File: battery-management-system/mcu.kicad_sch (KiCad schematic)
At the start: 44 parts, among them J16 I2C, J17 UART_INTERCONNECT, J18 LEDS, J19 CHARGE/DISCHARGE, J20 UART_USB, Q5 DMN3404L, U10 STC3100, U11 STM32L071CZTx, U7 ARM-JTAG-SWD, U8 AT24C512C, U9 NCT75DR2G

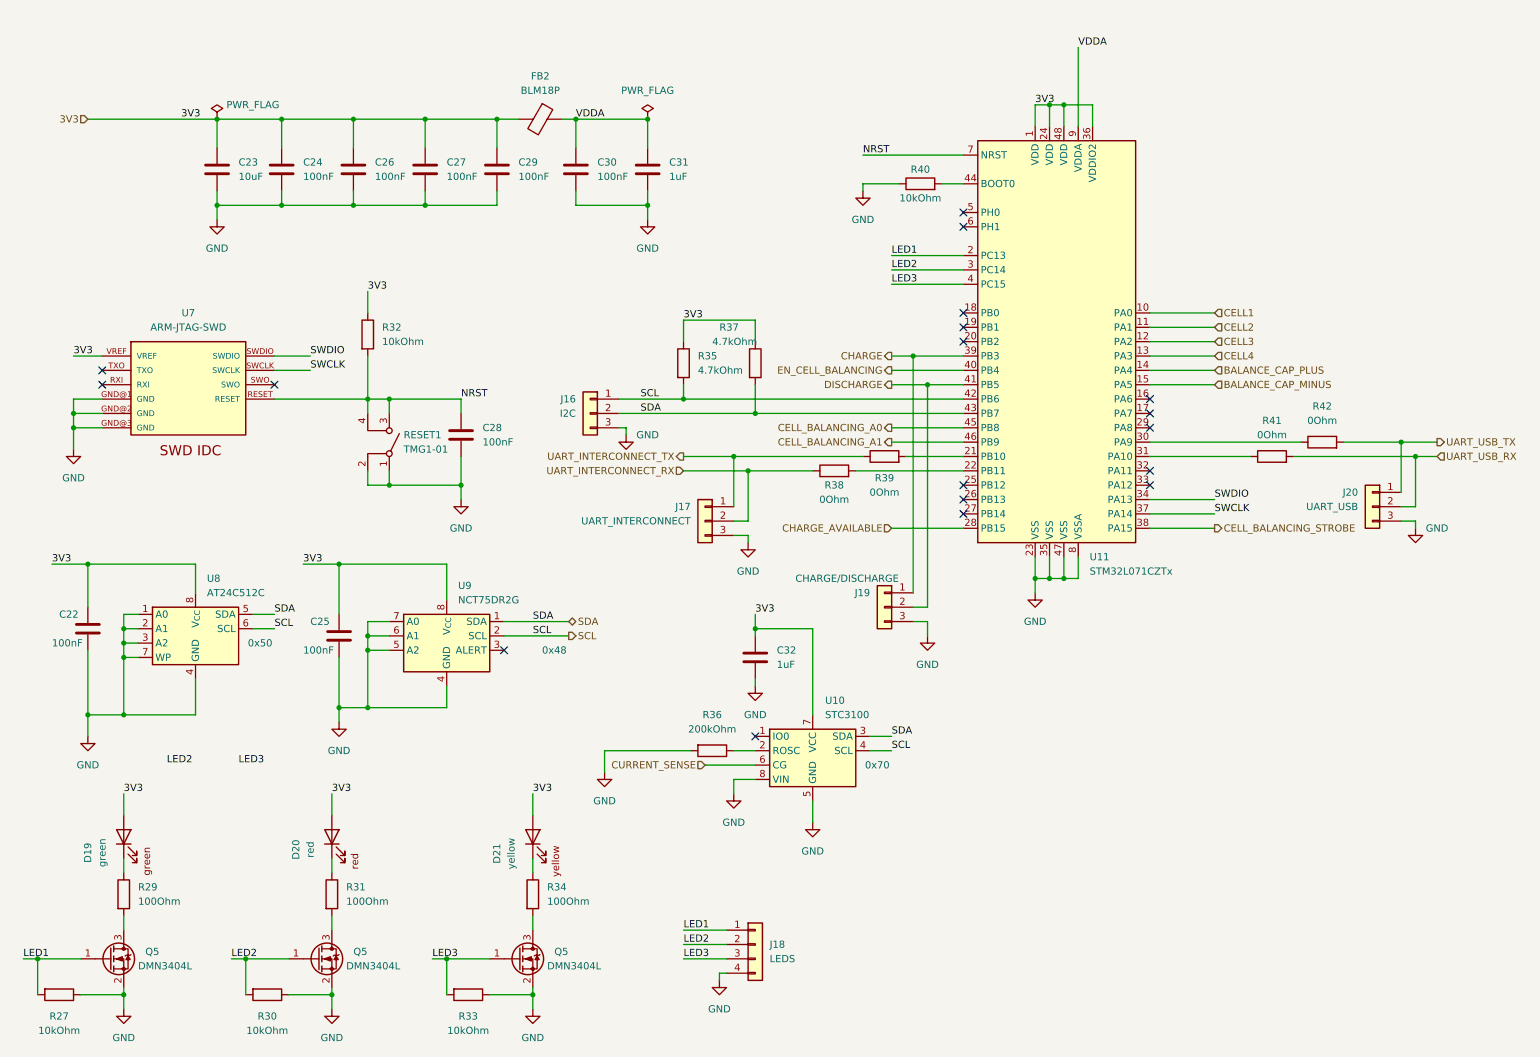
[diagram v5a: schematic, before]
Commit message: fix electrical rule check errors
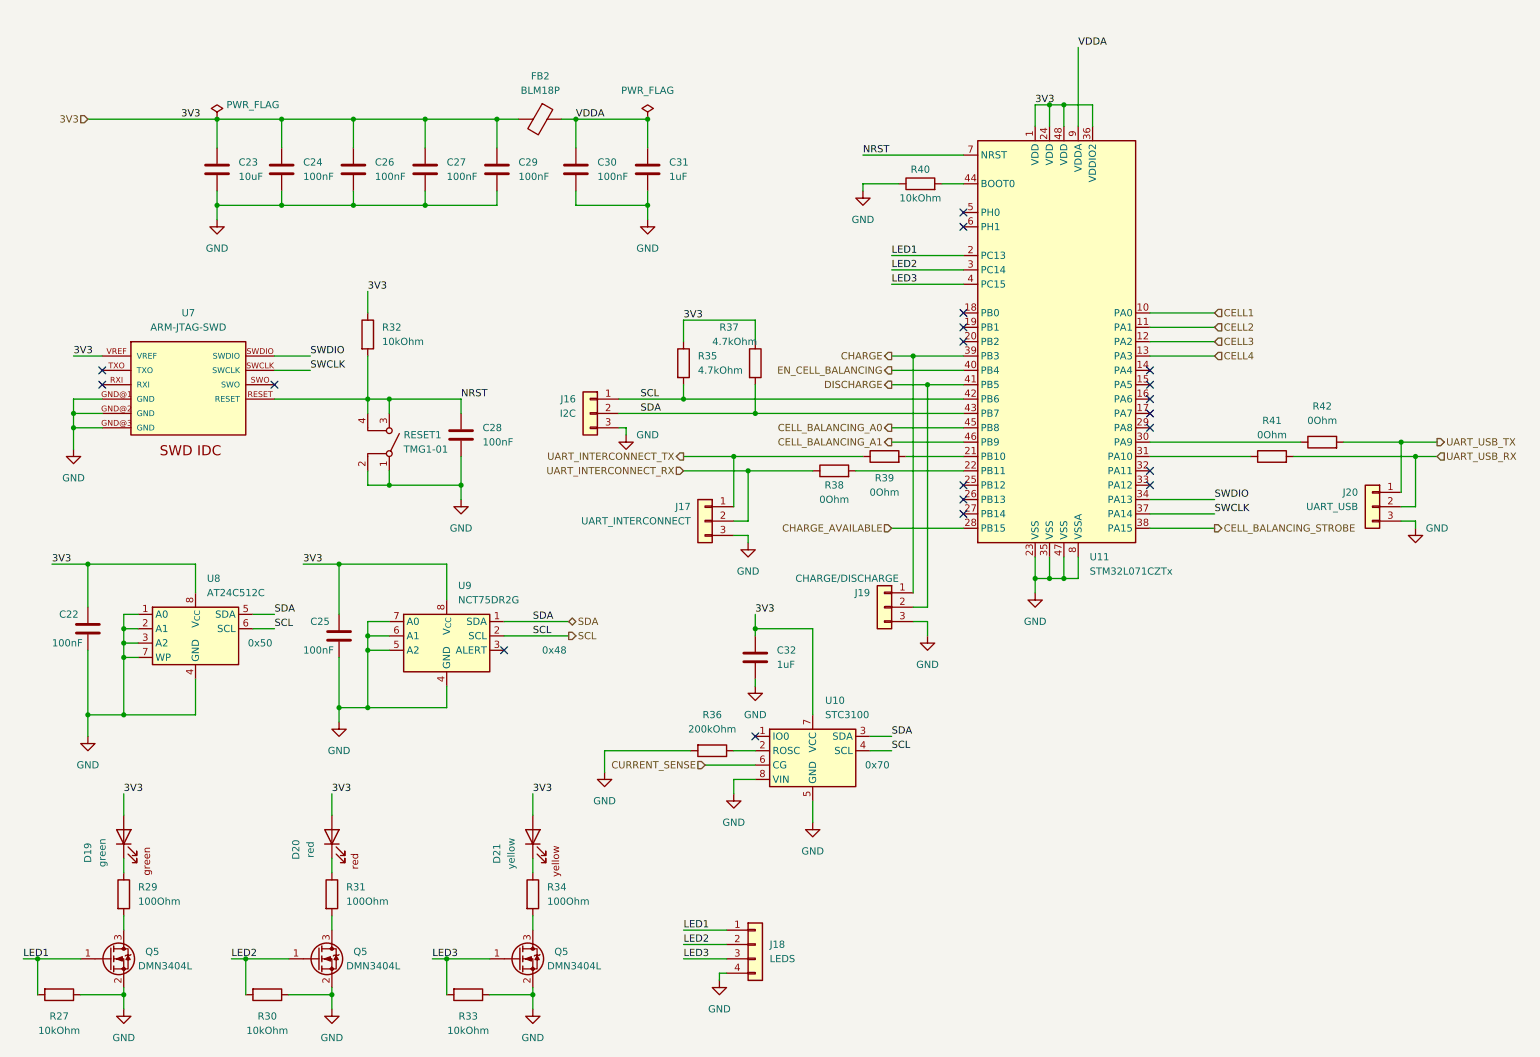
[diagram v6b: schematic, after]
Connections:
- net BALANCE_CAP_MINUS: no longer names the net of U11.15 (PA5)
- net BALANCE_CAP_PLUS: no longer names the net of U11.14 (PA4)
- no-connect marks 18 -> 20
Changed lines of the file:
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@@
   (no_connect (at 104.14 125.73))
   (no_connect (at 33.02 78.74))
+  (no_connect (at 218.44 76.2))
   (no_connect (at 218.44 86.36))
   (no_connect (at 185.42 48.26))
@@
   (no_connect (at 218.44 96.52))
   (no_connect (at 185.42 96.52))
+  (no_connect (at 218.44 78.74))
   (no_connect (at 185.42 66.04))
   (no_connect (at 185.42 50.8))
@@
     (stroke (width 0) (type default))
   )
-  (wire (pts (xy 218.44 78.74) (xy 229.87 78.74))
-    (stroke (width 0) (type default))
-  )
   (wire (pts (xy 158.75 121.92) (xy 158.75 137.16))
     (stroke (width 0) (type default))
@@
     (stroke (width 0) (type default))
   )
-  (wire (pts (xy 218.44 76.2) (xy 229.87 76.2))
-    (stroke (width 0) (type default))
-  )
   (wire (pts (xy 203.2 109.22) (xy 203.2 113.03))
     (stroke (width 0) (type default))
@@
     (effects (font (size 1.27 1.27)) (justify left bottom))
   )
-  (label "LED3" (at 57.15 146.05 0) (fields_autoplaced)
-    (effects (font (size 1.27 1.27)) (justify left bottom))
-  )
   (label "LED2" (at 55.88 180.34 0) (fields_autoplaced)
-    (effects (font (size 1.27 1.27)) (justify left bottom))
-  )
-  (label "LED2" (at 44.45 146.05 0) (fields_autoplaced)
     (effects (font (size 1.27 1.27)) (justify left bottom))
   )
@@
     (effects (font (size 1.27 1.27)) (justify left))
   )
-  (hierarchical_label "BALANCE_CAP_PLUS" (shape input) (at 229.87 76.2 0) (fields_autoplaced)
-    (effects (font (size 1.27 1.27)) (justify left))
-  )
   (hierarchical_label "3V3" (shape input) (at 30.48 31.75 180) (fields_autoplaced)
     (effects (font (size 1.27 1.27)) (justify right))
@@
     (effects (font (size 1.27 1.27)) (justify left))
   )
-  (hierarchical_label "BALANCE_CAP_MINUS" (shape input) (at 229.87 78.74 0) (fields_autoplaced)
-    (effects (font (size 1.27 1.27)) (justify left))
-  )

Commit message: add enable input for cell measurement
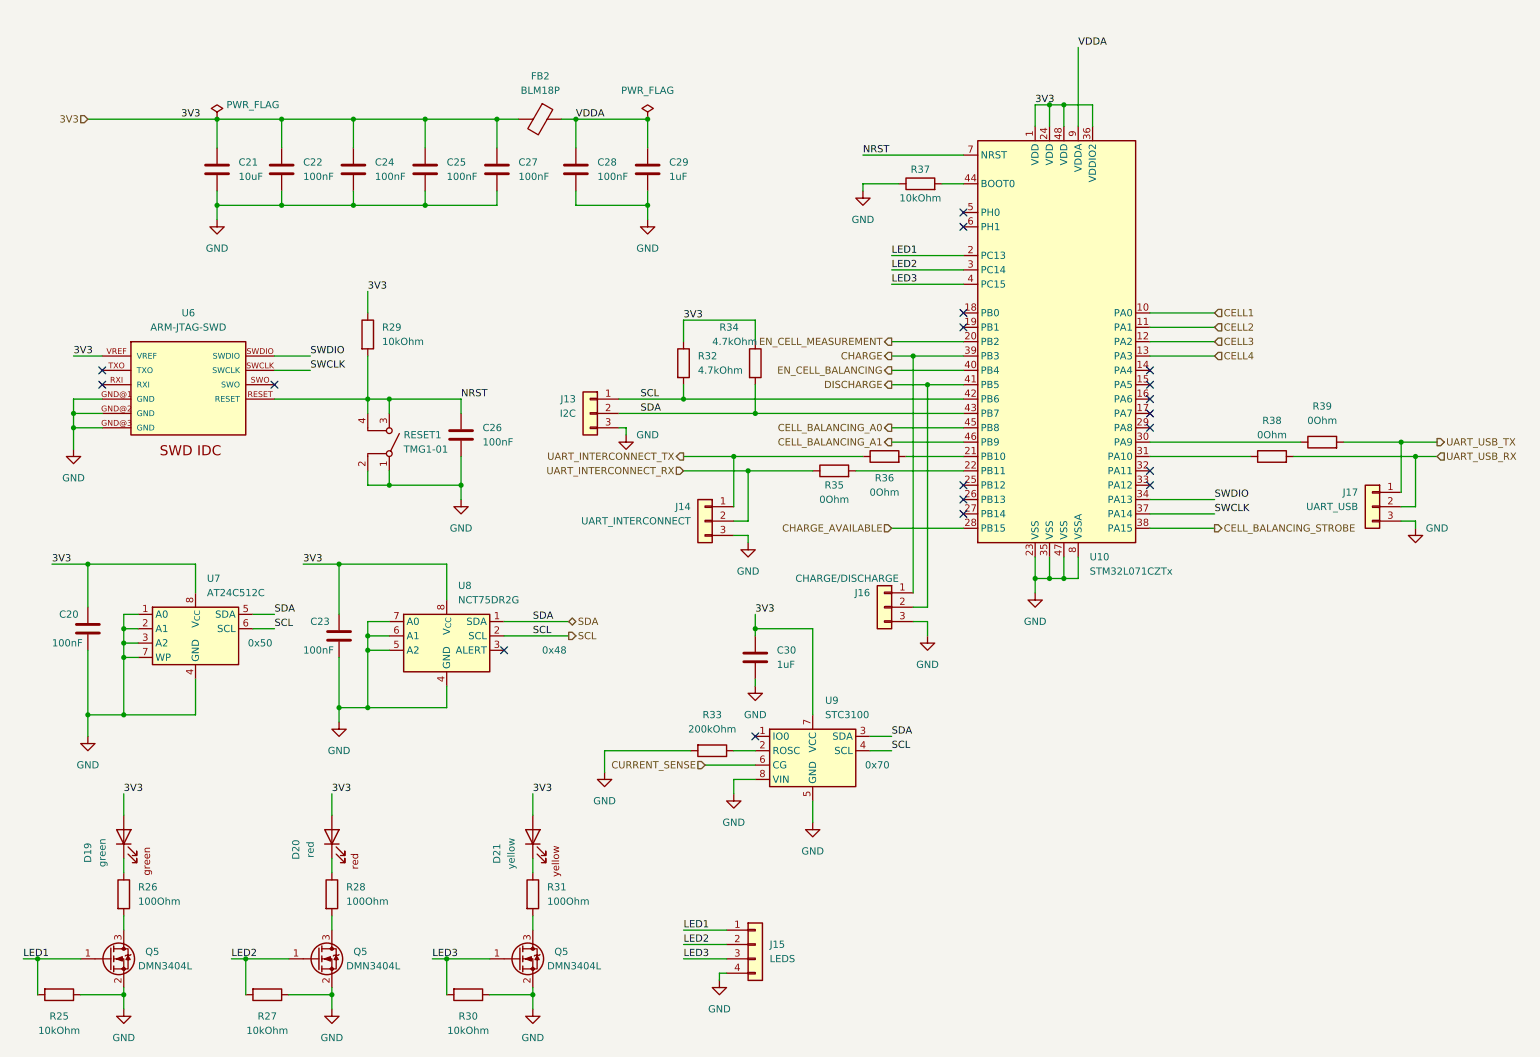
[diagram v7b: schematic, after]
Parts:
- renumbered C22 to C20, C23 to C21, C24 to C22, C25 to C23, C26 to C24, C27 to C25, C28 to C26, C29 to C27, C30 to C28, C31 to C29, C32 to C30, J16 to J13, J17 to J14, J18 to J15, J19 to J16, J20 to J17, R27 to R25, R29 to R26, R30 to R27, R31 to R28, R32 to R29, R33 to R30, R34 to R31, R35 to R32, R36 to R33, R37 to R34, R38 to R35, R39 to R36, R40 to R37, R41 to R38, R42 to R39, U11 to U10, U7 to U6, U8 to U7, U9 to U8, U10 to U9
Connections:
- net EN_CELL_MEASUREMENT: now reaches U10.20 (PB2)
- no-connect marks 20 -> 19

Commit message: improve layout
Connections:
- net LED1: now also U10.4 (PC15); no longer U10.2 (PC13)
- net LED3: now also U10.2 (PC13); no longer U10.4 (PC15)
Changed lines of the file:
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@@
+    (effects (font (size 1.27 1.27)) (justify left bottom))
+  )
+  (label "LED1" (at 172.72 60.96 0) (fields_autoplaced)
     (effects (font (size 1.27 1.27)) (justify left bottom))
   )
   (label "SCL" (at 109.22 123.19 0) (fields_autoplaced)
-    (effects (font (size 1.27 1.27)) (justify left bottom))
-  )
-  (label "LED1" (at 172.72 55.88 0) (fields_autoplaced)
     (effects (font (size 1.27 1.27)) (justify left bottom))
   )
@@
     (effects (font (size 1.27 1.27)) (justify left bottom))
   )
+  (label "LED3" (at 172.72 55.88 0) (fields_autoplaced)
+    (effects (font (size 1.27 1.27)) (justify left bottom))
+  )
   (label "LED1" (at 135.89 175.26 0) (fields_autoplaced)
     (effects (font (size 1.27 1.27)) (justify left bottom))
@@
     (effects (font (size 1.27 1.27)) (justify left bottom))
   )
-  (label "LED3" (at 172.72 60.96 0) (fields_autoplaced)
-    (effects (font (size 1.27 1.27)) (justify left bottom))
-  )
